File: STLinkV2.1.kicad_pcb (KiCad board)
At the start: 2 copper layers, 35.2 x 14.4 mm, 54 parts, among them J1 USB_C_USB2.0, J2 SWD, J3 USB_A, Q1 S8050, U1 RT9193-18GB, U2 USBLC6-2SC6, U3 STM32F103CBTx, Y1 8MHz

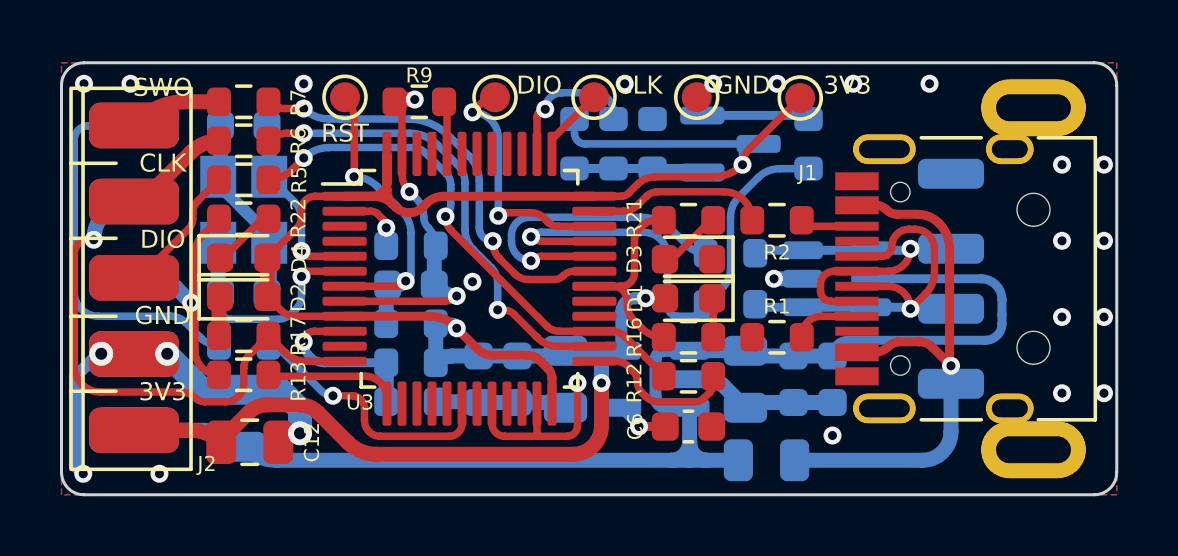
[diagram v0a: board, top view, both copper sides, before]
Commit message: Change board size and output connector.
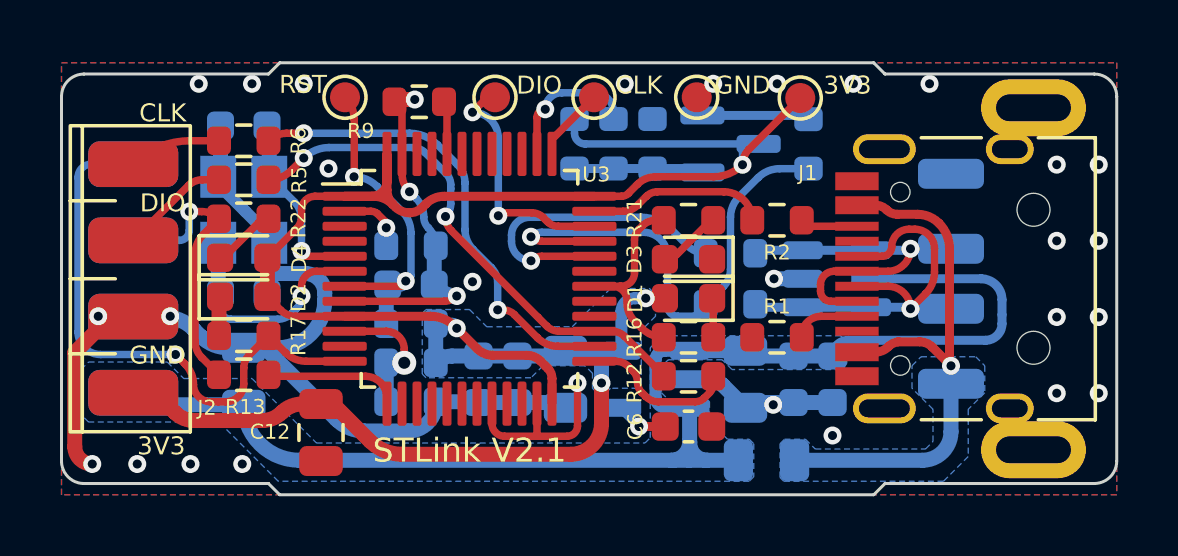
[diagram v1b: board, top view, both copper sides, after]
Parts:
- removed R11, R7: 100, Resistor_SMD:R_0603_1608Metric
- J2: footprint Conn_02x05_Horizontal_2Layer:Conn_02x05_Horizontal_2Layer -> Conn_Horizontal_2Layer:Conn_02x04_Horizontal_2Layer
- moved J2 2.52 mm to (186.3, 93.3)
- moved C12 2.40 mm to (193.9, 98.4), turned to 90 degrees
- moved C11 1.40 mm to (191.4, 96.5)
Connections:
- J2 pad 5: Net-(R7-Pad2) -> ST_TX
- J2 pad 6: Net-(R11-Pad1) -> ST_RX
- J2 pad 7: ST_TX -> GND
- J2 pad 8: ST_RX -> +5V
- U3 pad 18: O_RST -> unconnected-(U3-Pad18)
- U3 pad 31: O_SWO -> unconnected-(U3-Pad31)
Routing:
- net O_SWO: track 14.5 -> 0.00 mm, vias 2 -> 0
- net GND: track 53.9 -> 66.9 mm, vias 28 -> 31
- net Net-(R11-Pad1): track 12.9 -> 0.00 mm
- net O_RST: track 8.89 -> 0.00 mm, vias 1 -> 0
- net Net-(R7-Pad2): track 3.06 -> 0.00 mm
- net AIN: track 5.97 -> 4.66 mm
- net ST_TX: track 17.9 -> 19.1 mm
- net +5V: track 44.5 -> 45.3 mm
- net Net-(J2-Pad3): track 4.49 -> 3.66 mm
- net ST_RX: track 8.74 -> 9.50 mm
- net Net-(J2-Pad4): track 3.58 -> 3.05 mm
- added copper zone on B.Cu, net +3.3V
- added copper zone on B.Cu, net +5V
- added copper zone on B.Cu, net /VBUS
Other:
- outline, holes or cut-outs redrawn
- board text added: "STLink V2.1"
- board text removed: "SWO"

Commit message: Changed SWD connector to 02x04 2 layer.
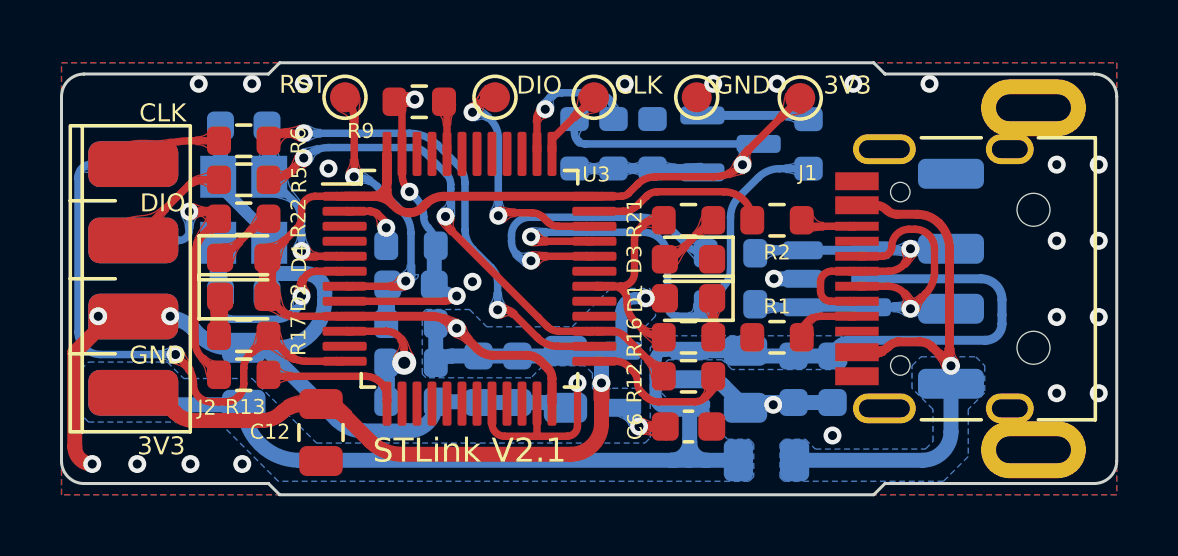
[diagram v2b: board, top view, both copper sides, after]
